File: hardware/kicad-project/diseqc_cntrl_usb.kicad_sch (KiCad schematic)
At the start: 5 parts, among them J5 USB4110-GF-A, U1 FT230XS

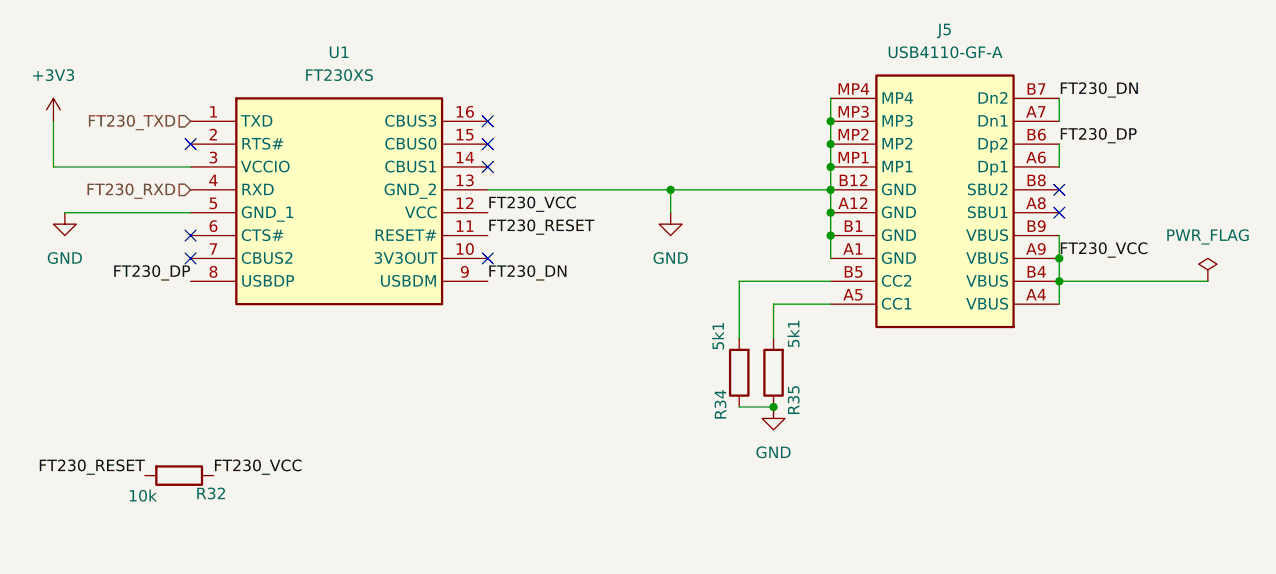
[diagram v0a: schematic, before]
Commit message: Starting v0.4 with FT230 fixes; extra TPs
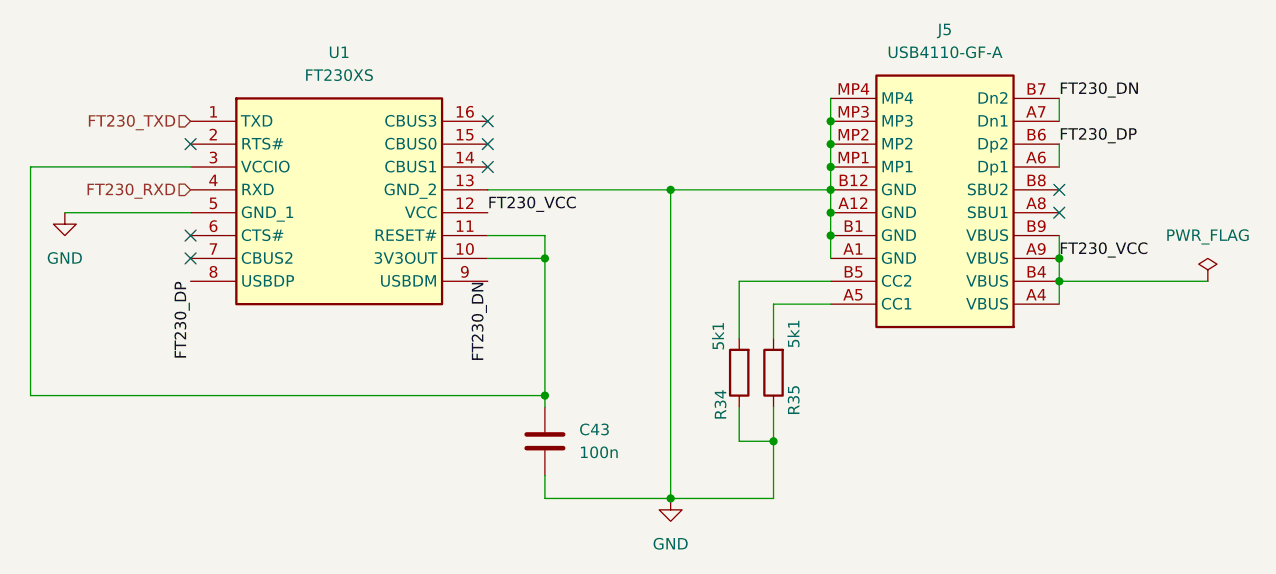
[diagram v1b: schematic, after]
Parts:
- removed R32: 10k, Resistor_SMD:R_0603_1608Metric_Pad0.98x0.95mm_HandSolder, symbol diseqc_cntrl:R
- added C43: 100n, Capacitor_SMD:C_0603_1608Metric_Pad1.08x0.95mm_HandSolder, symbol Device:C
- J5: InvenTree Part (none) -> J_USB-C_SKT_16P
- R34, R35: InvenTree Part (none) -> R_5k1_0603
- U1: InvenTree Part (none) -> IC_USB_UART_SSOP16
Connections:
- net +3V3 is gone; now on an unnamed net: U1.3 (VCCIO)
- net FT230_RESET is gone; now on an unnamed net: U1.11 (RESET#)
- net GND: now also C43.2
- net at U1.10 (3V3OUT): now also C43.1
- no-connect marks 9 -> 8

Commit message: Added FT230X decoupling (C44)
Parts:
- added C44: 10n, Capacitor_SMD:C_0603_1608Metric_Pad1.08x0.95mm_HandSolder, symbol Device:C
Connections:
- net FT230_VCC: now also C44.1
- net GND: now also C44.2
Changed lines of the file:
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@@
+	)
+	(junction
+		(at 105.41 86.36)
+		(diameter 0)
+		(color 0 0 0 0)
 	)
 	(junction
@@
 	)
 	(junction
+		(at 140.97 62.23)
+		(diameter 0)
+		(color 0 0 0 0)
+	)
+	(junction
 		(at 111.76 46.99)
 		(diameter 0)
@@
 	(wire
 		(pts
+			(xy 140.97 86.36) (xy 140.97 82.55)
+		)
+		(stroke
+			(width 0)
+			(type default)
+		)
+	)
+	(wire
+		(pts
 			(xy 80.01 59.69) (xy 80.01 74.93)
 		)
@@
 	(wire
 		(pts
-			(xy 137.16 62.23) (xy 153.67 62.23)
+			(xy 137.16 62.23) (xy 140.97 62.23)
 		)
 		(stroke
@@
 	(wire
 		(pts
+			(xy 140.97 62.23) (xy 140.97 74.93)
+		)
+		(stroke
+			(width 0)
+			(type default)
+		)
+	)
+	(wire
+		(pts
 			(xy 137.16 57.15) (xy 137.16 59.69)
 		)
@@
 	(wire
 		(pts
+			(xy 140.97 62.23) (xy 153.67 62.23)
+		)
+		(stroke
+			(width 0)
+			(type default)
+		)
+	)
+	(wire
+		(pts
 			(xy 93.98 86.36) (xy 105.41 86.36)
 		)
@@
 		(pts
 			(xy 73.66 59.69) (xy 80.01 59.69)
+		)
+		(stroke
+			(width 0)
+			(type default)
+		)
+	)
+	(wire
+		(pts
+			(xy 105.41 86.36) (xy 140.97 86.36)
 		)
 		(stroke
@@
 					(unit 1)
 				)
+			)
+		)
+	)
+	(symbol
+		(lib_id "Device:C")
+		(at 140.97 78.74 0)
+		(unit 1)
+		(body_style 1)
+		(exclude_from_sim no)
+		(in_bom yes)
+		(on_board yes)
+		(in_pos_files yes)
+		(dnp no)
+		(fields_autoplaced yes)
+		(property "Reference" "C44"
+			(at 144.78 77.4699 0)
+			(show_name no)
+			(do_not_autoplace no)
+			(effects
+				(font
+					(size 1.27 1.27)
+				)
+				(justify left)
+			)
+		)
+		(property "Value" "10n"
+			(at 144.78 80.0099 0)
+			(show_name no)
+			(do_not_autoplace no)
+			(effects
+				(font
+					(size 1.27 1.27)
+				)
+				(justify left)
+			)
+		)
+		(property "Footprint" "Capacitor_SMD:C_0603_1608Metric_Pad1.08x0.95mm_HandSolder"
+			(at 141.9352 82.55 0)
+			(hide yes)
+			(show_name no)
+			(do_not_autoplace no)
+			(effects
+				(font
+					(size 1.27 1.27)
+				)
+			)
+		)
+		(property "Datasheet" ""
+			(at 140.97 78.74 0)
+			(hide yes)
+			(show_name no)
+			(do_not_autoplace no)
+			(effects
+				(font
+					(size 1.27 1.27)
+				)
+			)
+		)
+		(property "Description" "Unpolarized capacitor"
+			(at 140.97 78.74 0)
+			(hide yes)
+			(show_name no)
+			(do_not_autoplace no)
+			(effects
+				(font
+					(size 1.27 1.27)
+				)
+			)
+		)
+		(property "InvenTree Part" "C_10n_0603"
+			(at 140.97 78.74 0)
+			(hide yes)
+			(show_name no)
+			(do_not_autoplace no)
+			(effects
+				(font
+					(size 1.27 1.27)
+				)
+			)
+		)
+		(property "KLC_S4.2_3V3OUT" ""
+			(at 140.97 78.74 0)
+			(hide yes)
+			(show_name no)
+			(do_not_autoplace no)
+			(effects
+				(font
+					(size 1.27 1.27)
+				)
+			)
+		)
+		(property "KLC_S4.2_VCC" ""
+			(at 140.97 78.74 0)
+			(hide yes)
+			(show_name no)
+			(do_not_autoplace no)
+			(effects
+				(font
+					(size 1.27 1.27)
+				)
+			)
+		)
+		(pin "1"
+		)
+		(pin "2"
+		)
+		(instances
+			(project "diseqc_cntrl"
+				(path "/82a905d8-f1d7-4995-9c16-94cf3cdcaad9/65fcf1a0-d0f2-4bf0-9977-67dd9f84afa5/e5108393-1145-4ace-bd05-28ed9bbcb2b1"
+					(reference "C44")
+					(unit 1)
+				)

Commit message: Added InvenTree part codes
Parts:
- C43: InvenTree (none) -> 75
- C44: InvenTree (none) -> 224
- J5: InvenTree (none) -> 82
- R34, R35: InvenTree (none) -> 111
- U1: InvenTree (none) -> 122
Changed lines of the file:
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@@
+			)
+		)
+		(property "Tolerance" ""
+			(at 105.41 72.39 90)
+			(hide yes)
+			(show_name no)
+			(do_not_autoplace no)
+			(effects
+				(font
+					(size 1.27 1.27)
+				)
+			)
+		)
+		(property "InvenTree" "111"
+			(at 105.41 72.39 90)
+			(hide yes)
+			(show_name no)
+			(do_not_autoplace no)
+			(effects
+				(font
+					(size 1.27 1.27)
+				)
 			)
 		)
@@
 			)
 		)
+		(property "Tolerance" ""
+			(at 80.01 80.01 0)
+			(hide yes)
+			(show_name no)
+			(do_not_autoplace no)
+			(effects
+				(font
+					(size 1.27 1.27)
+				)
+			)
+		)
+		(property "InvenTree" "75"
+			(at 80.01 80.01 0)
+			(hide yes)
+			(show_name no)
+			(do_not_autoplace no)
+			(effects
+				(font
+					(size 1.27 1.27)
+				)
+			)
+		)
 		(pin "1"
 		)
@@
 			)
 		)
+		(property "Tolerance" ""
+			(at 140.97 78.74 0)
+			(hide yes)
+			(show_name no)
+			(do_not_autoplace no)
+			(effects
+				(font
+					(size 1.27 1.27)
+				)
+			)
+		)
+		(property "InvenTree" "224"
+			(at 140.97 78.74 0)
+			(hide yes)
+			(show_name no)
+			(do_not_autoplace no)
+			(effects
+				(font
+					(size 1.27 1.27)
+				)
+			)
+		)
 		(pin "1"
 		)
@@
 			)
 		)
+		(property "Tolerance" ""
+			(at 40.64 44.45 0)
+			(hide yes)
+			(show_name no)
+			(do_not_autoplace no)
+			(effects
+				(font
+					(size 1.27 1.27)
+				)
+			)
+		)
+		(property "InvenTree" "122"
+			(at 40.64 44.45 0)
+			(hide yes)
+			(show_name no)
+			(do_not_autoplace no)
+			(effects
+				(font
+					(size 1.27 1.27)
+				)
+			)
+		)
 		(pin "8"
 		)
@@
 		)
 		(property "KLC_S4.2_VCC" ""
+			(at 101.6 72.39 90)
+			(hide yes)
+			(show_name no)
+			(do_not_autoplace no)
+			(effects
+				(font
+					(size 1.27 1.27)
+				)
+			)
+		)
+		(property "Tolerance" ""
+			(at 101.6 72.39 90)
+			(hide yes)
+			(show_name no)
+			(do_not_autoplace no)
+			(effects
+				(font
+					(size 1.27 1.27)
+				)
+			)
+		)
+		(property "InvenTree" "111"
 			(at 101.6 72.39 90)
 			(hide yes)
@@
 			(at 137.16 64.77 0)
 			(hide yes)
+			(show_name no)
+			(do_not_autoplace no)
+			(effects
+				(font
+					(size 1.27 1.27)
+				)
+			)
+		)
+		(property "Tolerance" ""
+			(at 137.16 64.77 0)
+			(hide yes)
+			(show_name no)
+			(do_not_autoplace no)
+			(effects
+				(font
+					(size 1.27 1.27)
+				)
+			)
+		)
+		(property "InvenTree" "82"
+			(at 137.16 64.77 0)
+			(hide yes)

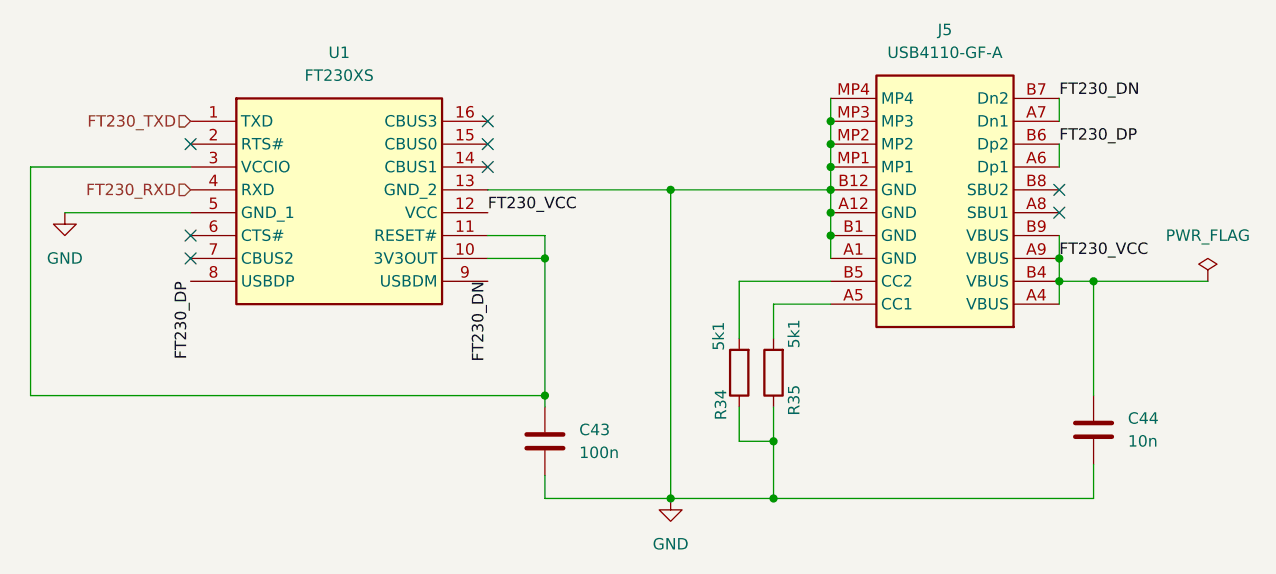
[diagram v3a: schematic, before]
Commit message: nwe board laylout for LAN8742A
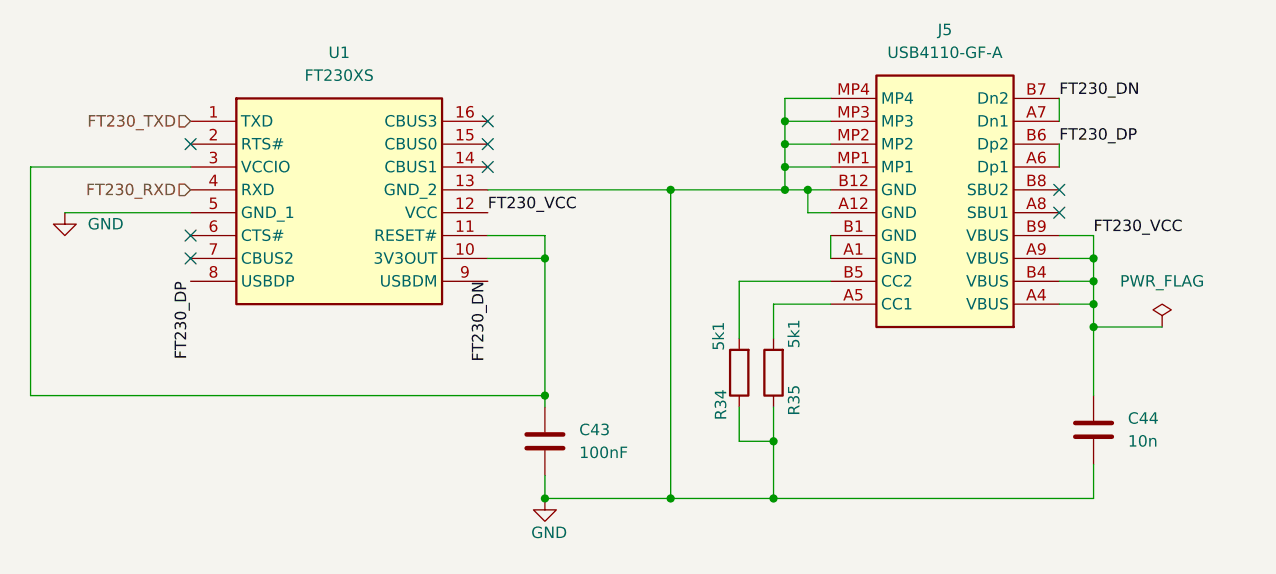
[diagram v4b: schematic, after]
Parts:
- C43: value 100n -> 100nF
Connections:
- net GND: no longer J5.A1 (GND), J5.B1 (GND)
- new net: J5.A1 (GND), J5.B1 (GND)

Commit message: Added MCU decoupling
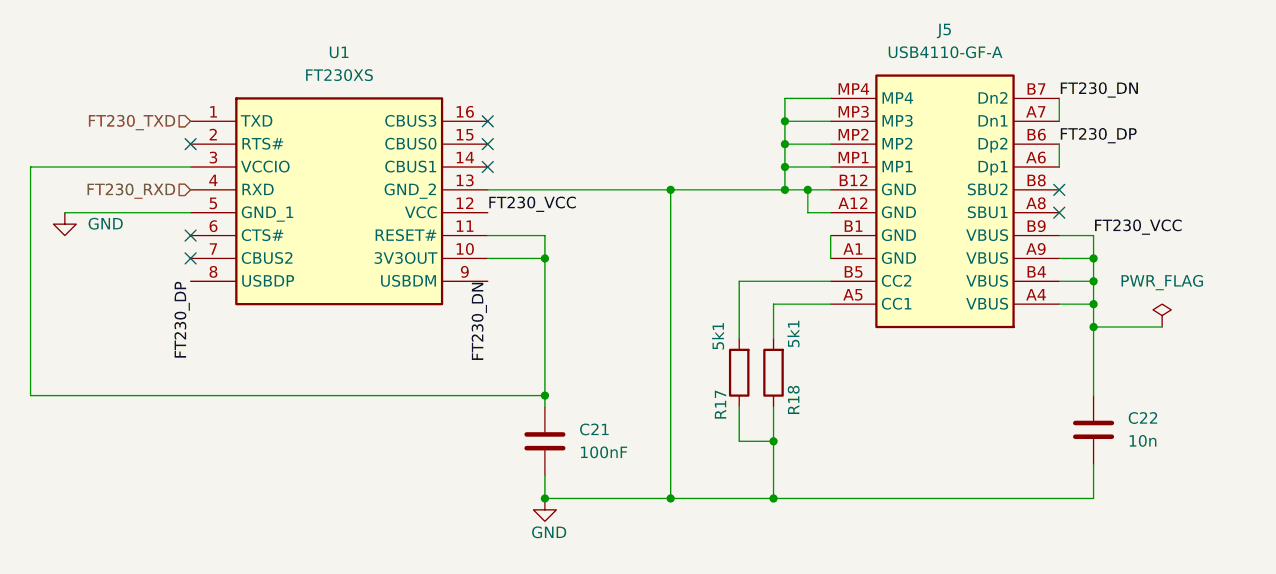
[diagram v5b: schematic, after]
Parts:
- renumbered C43 to C21, C44 to C22, R34 to R17, R35 to R18
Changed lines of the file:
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@@
 		(dnp no)
 		(fields_autoplaced yes)
-		(property "Reference" "#PWR066"
+		(property "Reference" "#PWR042"
 			(at 26.67 60.96 0)
 			(hide yes)
@@
 			(project "diseqc_cntrl"
 				(path "/82a905d8-f1d7-4995-9c16-94cf3cdcaad9/65fcf1a0-d0f2-4bf0-9977-67dd9f84afa5/e5108393-1145-4ace-bd05-28ed9bbcb2b1"
-					(reference "#PWR066")
+					(reference "#PWR042")
 					(unit 1)
 				)
@@
 		(in_pos_files yes)
 		(dnp no)
-		(property "Reference" "#PWR065"
+		(property "Reference" "#PWR043"
 			(at 80.01 92.71 0)
 			(hide yes)
@@
 			(project "diseqc_cntrl"
 				(path "/82a905d8-f1d7-4995-9c16-94cf3cdcaad9/65fcf1a0-d0f2-4bf0-9977-67dd9f84afa5/e5108393-1145-4ace-bd05-28ed9bbcb2b1"
-					(reference "#PWR065")
+					(reference "#PWR043")
 					(unit 1)
 				)
@@
 		(in_pos_files yes)
 		(dnp no)
-		(property "Reference" "R35"
+		(property "Reference" "R18"
 			(at 107.696 75.438 90)
 			(show_name no)
@@
 			(project "diseqc_cntrl"
 				(path "/82a905d8-f1d7-4995-9c16-94cf3cdcaad9/65fcf1a0-d0f2-4bf0-9977-67dd9f84afa5/e5108393-1145-4ace-bd05-28ed9bbcb2b1"
-					(reference "R35")
+					(reference "R18")
 					(unit 1)
 				)
@@
 		(dnp no)
 		(fields_autoplaced yes)
-		(property "Reference" "C43"
+		(property "Reference" "C21"
 			(at 83.82 78.7399 0)
 			(show_name no)
@@
 			(project "diseqc_cntrl"
 				(path "/82a905d8-f1d7-4995-9c16-94cf3cdcaad9/65fcf1a0-d0f2-4bf0-9977-67dd9f84afa5/e5108393-1145-4ace-bd05-28ed9bbcb2b1"
-					(reference "C43")
+					(reference "C21")
 					(unit 1)
 				)
@@
 		(dnp no)
 		(fields_autoplaced yes)
-		(property "Reference" "C44"
+		(property "Reference" "C22"
 			(at 144.78 77.4699 0)
 			(show_name no)
@@
 			(project "diseqc_cntrl"
 				(path "/82a905d8-f1d7-4995-9c16-94cf3cdcaad9/65fcf1a0-d0f2-4bf0-9977-67dd9f84afa5/e5108393-1145-4ace-bd05-28ed9bbcb2b1"
-					(reference "C44")
+					(reference "C22")
 					(unit 1)
 				)
@@
 		(in_pos_files yes)
 		(dnp no)
-		(property "Reference" "R34"
+		(property "Reference" "R17"
 			(at 99.568 75.946 90)
 			(show_name no)
@@
 			(project "diseqc_cntrl"
 				(path "/82a905d8-f1d7-4995-9c16-94cf3cdcaad9/65fcf1a0-d0f2-4bf0-9977-67dd9f84afa5/e5108393-1145-4ace-bd05-28ed9bbcb2b1"
-					(reference "R34")
+					(reference "R17")
 					(unit 1)
 				)

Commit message: v0.5 routing complete
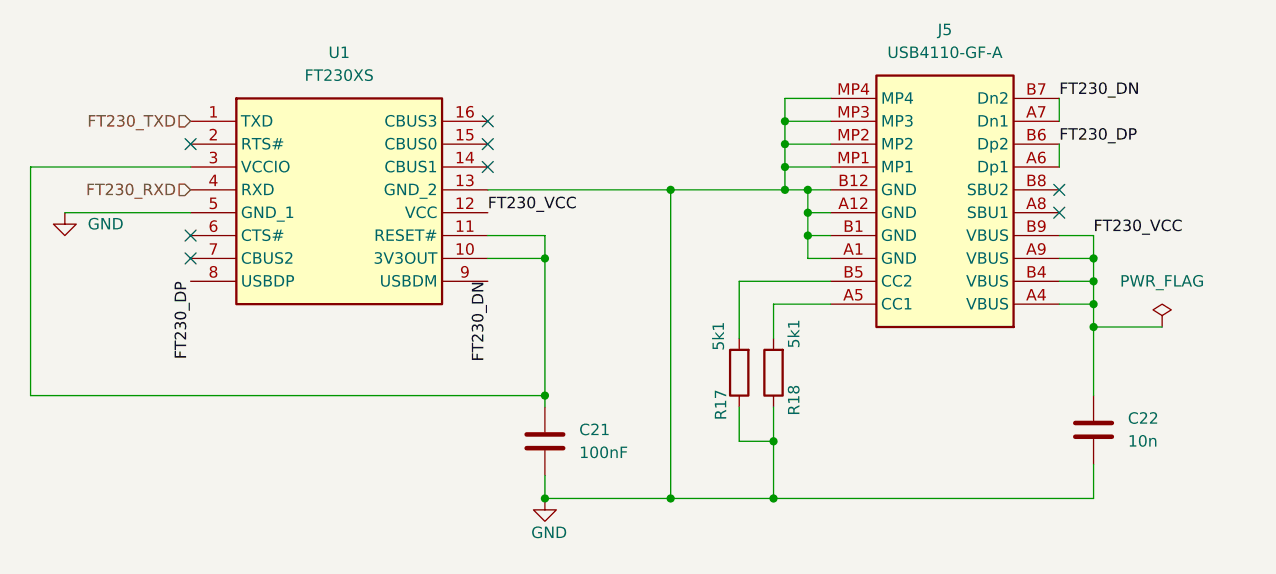
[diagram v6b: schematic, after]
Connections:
- net GND: now also J5.A1 (GND), J5.B1 (GND)
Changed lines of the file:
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@@
 	(paper "A4")
 	(junction
+		(at 109.22 57.15)
+		(diameter 0)
+		(color 0 0 0 0)
+	)
+	(junction
 		(at 93.98 86.36)
 		(diameter 0)
@@
 	)
 	(junction
+		(at 109.22 54.61)
+		(diameter 0)
+		(color 0 0 0 0)
+	)
+	(junction
 		(at 140.97 62.23)
 		(diameter 0)
@@
 	(wire
 		(pts
+			(xy 109.22 59.69) (xy 109.22 57.15)
+		)
+		(stroke
+			(width 0)
+			(type default)
+		)
+	)
+	(wire
+		(pts
 			(xy 140.97 62.23) (xy 140.97 67.31)
 		)
@@
 	(wire
 		(pts
+			(xy 109.22 57.15) (xy 109.22 54.61)
+		)
+		(stroke
+			(width 0)
+			(type default)
+		)
+	)
+	(wire
+		(pts
 			(xy 111.76 41.91) (xy 106.68 41.91)
 		)
@@
 	(wire
 		(pts
+			(xy 111.76 59.69) (xy 109.22 59.69)
+		)
+		(stroke
+			(width 0)
+			(type default)
+		)
+	)
+	(wire
+		(pts
 			(xy 93.98 86.36) (xy 105.41 86.36)
 		)
@@
 	(wire
 		(pts
-			(xy 111.76 57.15) (xy 111.76 59.69)
-		)
-		(stroke
-			(width 0)
-			(type default)
-		)
-	)
-	(wire
-		(pts
 			(xy 106.68 46.99) (xy 111.76 46.99)
 		)
@@
 		)
 		(stroke
+			(width 0)
+			(type default)
+		)
+	)
+	(wire
+		(pts
+			(xy 111.76 57.15) (xy 109.22 57.15)
+		)
+		(stroke
